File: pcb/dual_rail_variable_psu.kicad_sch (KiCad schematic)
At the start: 22 parts, among them U15 OPA140, U16 OPA1611, U4 OPA1611, U8 DAC8551

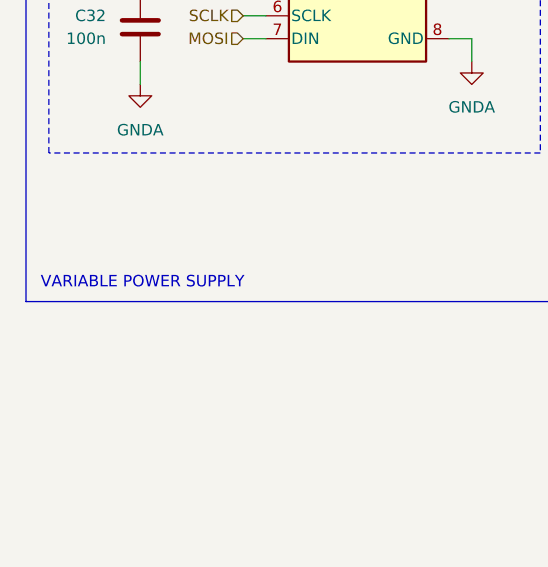
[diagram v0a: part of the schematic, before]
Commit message: rework to tia feedback selection, board power, and ui
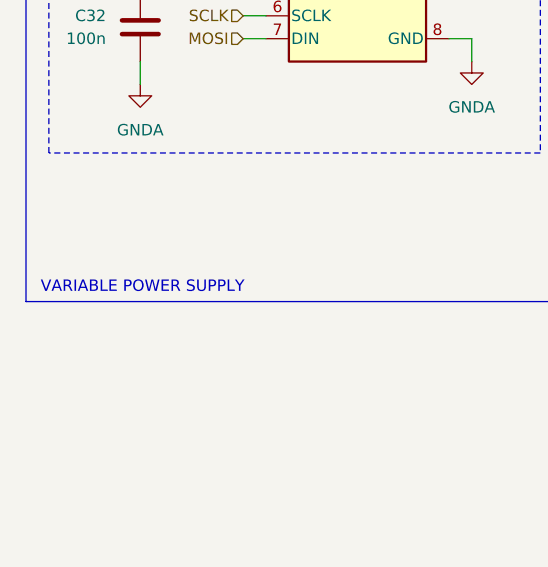
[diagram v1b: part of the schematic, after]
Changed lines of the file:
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@@
 	(text "VARIABLE POWER SUPPLY"
 		(exclude_from_sim no)
-		(at 73.914 157.988 0)
+		(at 73.914 158.496 0)
 		(effects
 			(font
